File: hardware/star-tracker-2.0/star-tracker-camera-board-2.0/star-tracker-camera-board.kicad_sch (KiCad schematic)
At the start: 41 parts, among them J1 3-1734742-6, U1 AR0134CSSM00SPCA0, U2 TPS70618DRVR, U3 TPS71928-28DRVT, U4 TPS71928-28DRVT, X1 MC2520Z27.0000C19XSH

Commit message: Update to Camera Board
Update BOM for camera board, replaced lower tier dielectric caps to X7R
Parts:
- C1: DIS Digikey -> Mouser; DPN 399-19365-1-ND -> 81-GXT155R71E103KE1D; MFR KEMET -> Murata; MPN C0402C103J5RACAUTO -> GXT155R71E103KE01D
- C11, C13, C7, C8, C9: DIS Digikey -> Mouser; DPN 399-17548-1-ND -> 80-C0402C104J4RAUTO
- C2, C3, C4, C5, C6: DIS Digikey -> Mouser; DPN 490-12286-1-ND -> 80-C0603C106J3RACTU; MFR Murata Electronics -> KEMET; MPN GRT188C81C106ME13D -> C0603C106J3RACTU
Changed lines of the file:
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@@
 			)
 		)
-		(property "Description" "10000 pF ±5% 50V Ceramic Capacitor X7R 0402 (1005 Metric)"
+		(property "Description" "0.01uF 10% 25VDC Ceramic Capacitor X7R 0402 (1005 Metric)"
 			(at 58.42 68.58 0)
 			(hide yes)
@@
 			)
 		)
-		(property "DIS" "Digikey"
+		(property "DIS" "Mouser"
 			(at 58.42 68.58 0)
 			(hide yes)
@@
 			)
 		)
-		(property "DPN" "399-19365-1-ND"
+		(property "DPN" "81-GXT155R71E103KE1D "
 			(at 58.42 68.58 0)
 			(hide yes)
@@
 			)
 		)
-		(property "MFR" "KEMET"
+		(property "MFR" "Murata"
 			(at 58.42 68.58 0)
 			(hide yes)
@@
 			)
 		)
-		(property "MPN" "C0402C103J5RACAUTO"
+		(property "MPN" "GXT155R71E103KE01D"
 			(at 58.42 68.58 0)
 			(hide yes)
@@
 			)
 		)
-		(property "Description" "10 µF ±20% 16V Ceramic Capacitor X6S 0603 (1608 Metric)"
+		(property "Description" "10 µF ±5% 23V Ceramic Capacitor X7R 0603 (1608 Metric)"
 			(at 314.96 50.8 0)
 			(hide yes)
@@
 			)
 		)
-		(property "DIS" "Digikey"
+		(property "DIS" "Mouser"
 			(at 314.96 50.8 0)
 			(hide yes)
@@
 			)
 		)
-		(property "DPN" "490-12286-1-ND"
+		(property "DPN" "80-C0603C106J3RACTU"
 			(at 314.96 50.8 0)
 			(hide yes)
@@
 			)
 		)
-		(property "MFR" "Murata Electronics"
+		(property "MFR" "KEMET"
 			(at 314.96 50.8 0)
 			(hide yes)
@@
 			)
 		)
-		(property "MPN" "GRT188C81C106ME13D"
+		(property "MPN" "C0603C106J3RACTU "
 			(at 314.96 50.8 0)
 			(hide yes)
@@
 			)
 		)
-		(property "DIS" "Digikey"
+		(property "DIS" "Mouser"
 			(at 368.3 50.8 0)
 			(hide yes)
@@
 			)
 		)
-		(property "DPN" "399-17548-1-ND"
+		(property "DPN" "80-C0402C104J4RAUTO "
 			(at 368.3 50.8 0)
 			(hide yes)
@@
 			)
 		)
-		(property "Description" "10 µF ±20% 16V Ceramic Capacitor X6S 0603 (1608 Metric)"
+		(property "Description" "10 µF ±5% 23V Ceramic Capacitor X7R 0603 (1608 Metric)"
 			(at 304.8 50.8 0)
 			(hide yes)
@@
 			)
 		)
-		(property "DIS" "Digikey"
+		(property "DIS" "Mouser"
 			(at 304.8 50.8 0)
 			(hide yes)
@@
 			)
 		)
-		(property "DPN" "490-12286-1-ND"
+		(property "DPN" "80-C0603C106J3RACTU"
 			(at 304.8 50.8 0)
 			(hide yes)
@@
 			)
 		)
-		(property "MFR" "Murata Electronics"
+		(property "MFR" "KEMET"
 			(at 304.8 50.8 0)
 			(hide yes)
@@
 			)
 		)
-		(property "MPN" "GRT188C81C106ME13D"
+		(property "MPN" "C0603C106J3RACTU "
 			(at 304.8 50.8 0)
 			(hide yes)
@@
 			)
 		)
-		(property "Description" "10 µF ±20% 16V Ceramic Capacitor X6S 0603 (1608 Metric)"
+		(property "Description" "10 µF ±5% 23V Ceramic Capacitor X7R 0603 (1608 Metric)"
 			(at 284.48 50.8 0)
 			(hide yes)
@@
 			)
 		)
-		(property "DIS" "Digikey"
+		(property "DIS" "Mouser"
 			(at 284.48 50.8 0)
 			(hide yes)
@@
 			)
 		)
-		(property "DPN" "490-12286-1-ND"
+		(property "DPN" "80-C0603C106J3RACTU"
 			(at 284.48 50.8 0)
 			(hide yes)
@@
 			)
 		)
-		(property "MFR" "Murata Electronics"
+		(property "MFR" "KEMET"
 			(at 284.48 50.8 0)
 			(hide yes)
@@
 			)
 		)
-		(property "MPN" "GRT188C81C106ME13D"
+		(property "MPN" "C0603C106J3RACTU "
 			(at 284.48 50.8 0)
 			(hide yes)
@@
 			)
 		)
-		(property "DIS" "Digikey"
+		(property "DIS" "Mouser"
 			(at 327.66 50.8 0)
 			(hide yes)
@@
 			)
 		)
-		(property "DPN" "399-17548-1-ND"
+		(property "DPN" "80-C0402C104J4RAUTO "
 			(at 327.66 50.8 0)
 			(hide yes)
@@
 			)
 		)
-		(property "Description" "10 µF ±20% 16V Ceramic Capacitor X6S 0603 (1608 Metric)"
+		(property "Description" "10 µF ±5% 23V Ceramic Capacitor X7R 0603 (1608 Metric)"
 			(at 274.32 50.8 0)
 			(hide yes)
@@
 			)
 		)
-		(property "DIS" "Digikey"
+		(property "DIS" "Mouser"
 			(at 274.32 50.8 0)
 			(hide yes)
@@
 			)
 		)
-		(property "DPN" "490-12286-1-ND"
+		(property "DPN" "80-C0603C106J3RACTU"
 			(at 274.32 50.8 0)
 			(hide yes)
@@
 			)
 		)
-		(property "MFR" "Murata Electronics"
+		(property "MFR" "KEMET"
 			(at 274.32 50.8 0)
 			(hide yes)
@@
 			)
 		)
-		(property "MPN" "GRT188C81C106ME13D"
+		(property "MPN" "C0603C106J3RACTU "
 			(at 274.32 50.8 0)
 			(hide yes)
@@
 			)
 		)
-		(property "Description" "10 µF ±20% 16V Ceramic Capacitor X6S 0603 (1608 Metric)"
+		(property "Description" "10 µF ±5% 23V Ceramic Capacitor X7R 0603 (1608 Metric)"
 			(at 294.64 50.8 0)
 			(hide yes)
@@
 			)
 		)
-		(property "DIS" "Digikey"
+		(property "DIS" "Mouser"
 			(at 294.64 50.8 0)
 			(hide yes)
@@
 			)
 		)
-		(property "DPN" "490-12286-1-ND"
+		(property "DPN" "80-C0603C106J3RACTU"
 			(at 294.64 50.8 0)
 			(hide yes)
@@
 			)
 		)
-		(property "MFR" "Murata Electronics"
+		(property "MFR" "KEMET"
 			(at 294.64 50.8 0)
 			(hide yes)
@@
 			)
 		)
-		(property "MPN" "GRT188C81C106ME13D"
+		(property "MPN" "C0603C106J3RACTU "
 			(at 294.64 50.8 0)
 			(hide yes)
@@
 			)
 		)
-		(property "DIS" "Digikey"
+		(property "DIS" "Mouser"
 			(at 358.14 50.8 0)
 			(hide yes)
@@
 			)
 		)
-		(property "DPN" "399-17548-1-ND"
+		(property "DPN" "80-C0402C104J4RAUTO "
 			(at 358.14 50.8 0)
 			(hide yes)
@@
 			)
 		)
-		(property "DIS" "Digikey"
+		(property "DIS" "Mouser"
 			(at 337.82 50.8 0)
 			(hide yes)
@@
 			)
 		)
-		(property "DPN" "399-17548-1-ND"
+		(property "DPN" "80-C0402C104J4RAUTO "
 			(at 337.82 50.8 0)
 			(hide yes)
@@
 			)
 		)
-		(property "DIS" "Digikey"
+		(property "DIS" "Mouser"
 			(at 347.98 50.8 0)
 			(hide yes)
@@
 			)
 		)
-		(property "DPN" "399-17548-1-ND"
+		(property "DPN" "80-C0402C104J4RAUTO "
 			(at 347.98 50.8 0)
 			(hide yes)

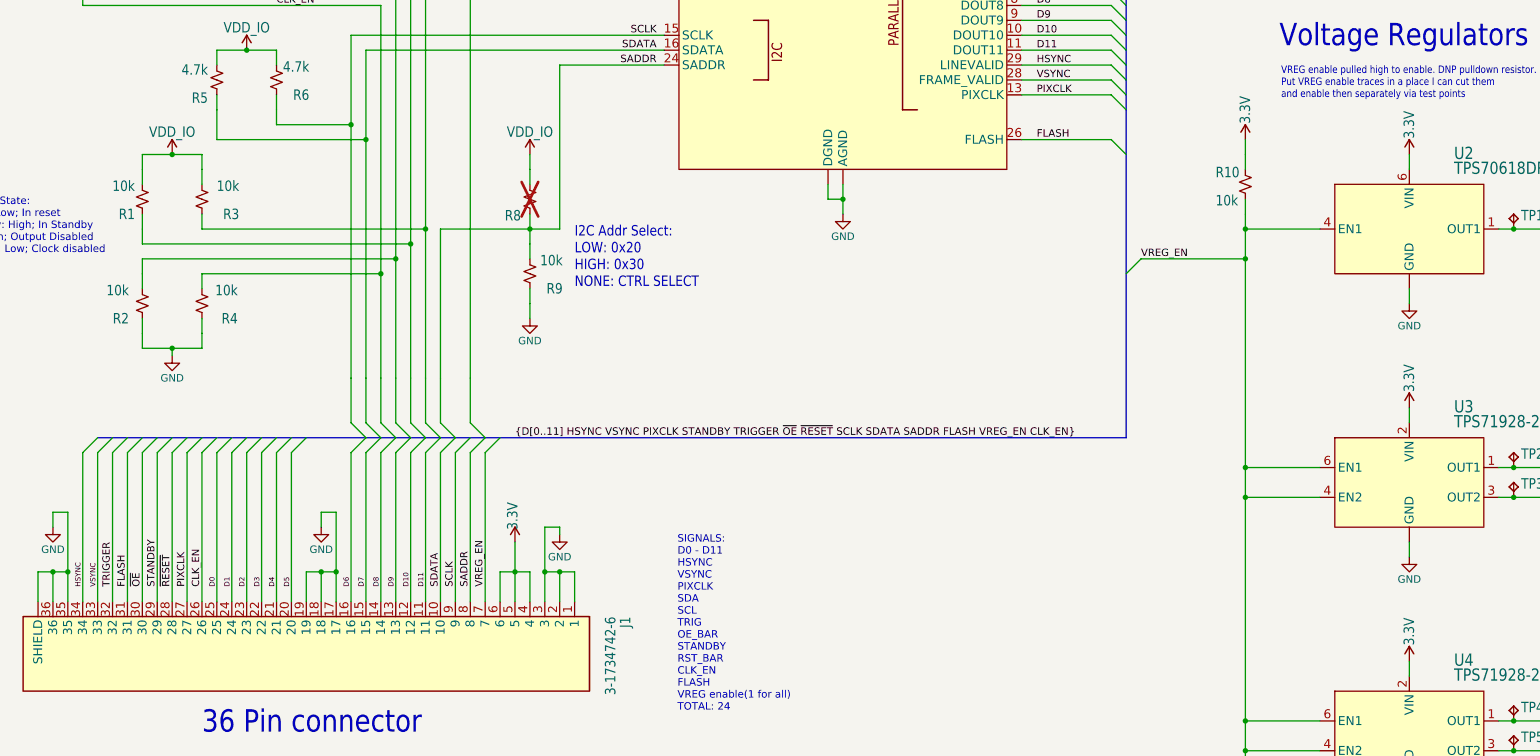
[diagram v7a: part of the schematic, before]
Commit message: Finishing touches
added gitignore for .ds_store (mac file for kicad) changed bom details for components. added 3d models to footprints. Went over schematic checklist. Camera and star tracker ready for final DR for send off.
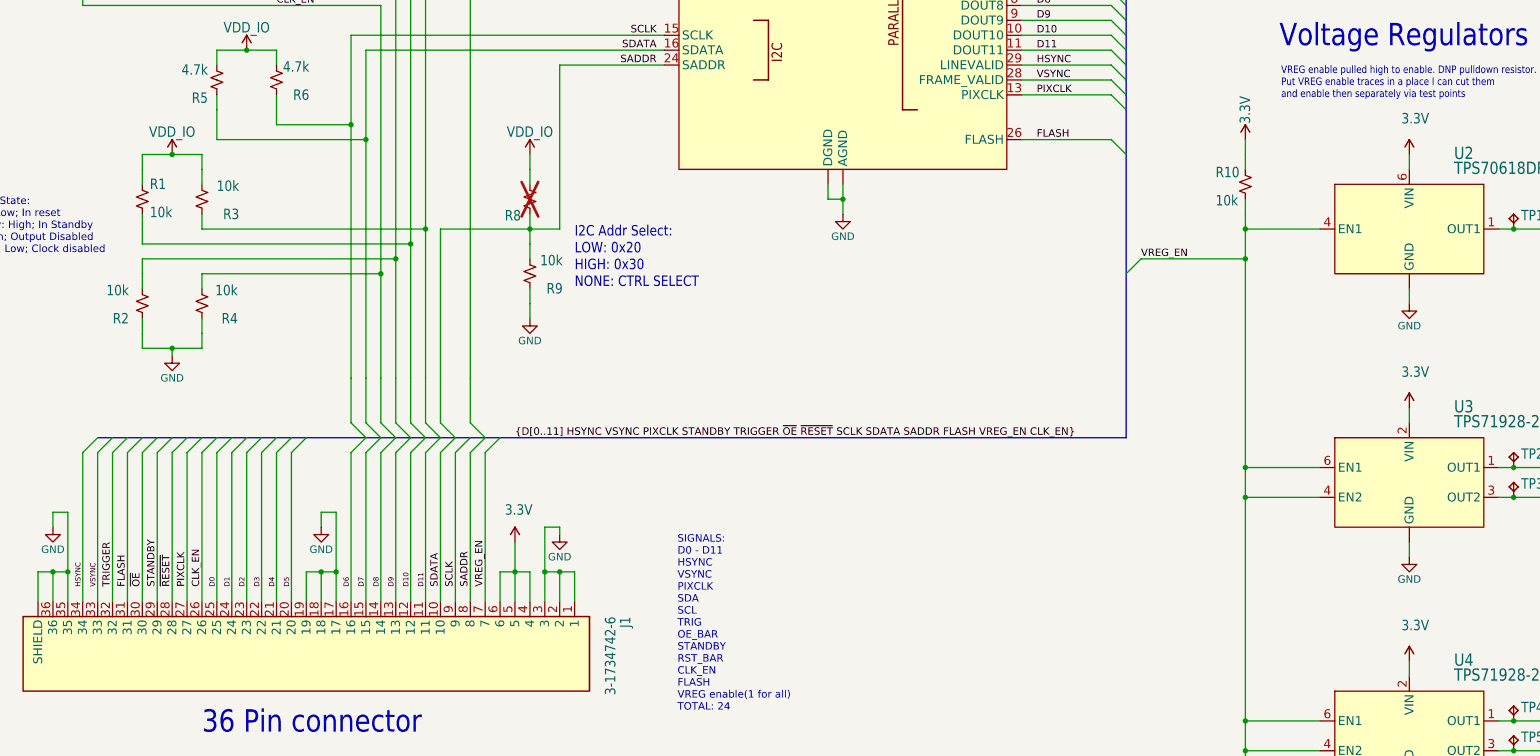
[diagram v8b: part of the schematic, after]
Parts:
- C10, C12, C15, C17, C19: DIS DigiKey -> Mouser; DPN 490-GRT188C71E225KE13DCT-ND -> 81-GRT188C71E225KE3D
- C14, C16, C18: DIS DigiKey -> Mouser; DPN 490-18215-1-ND -> 81-GRT155C81E105KE3D
- J1: DPN A100241CT-ND -> 17-3-2492144-6TR-ND; MPN 3-1734742-6 -> 3-2492144-6
- R1, R10, R2, R3, R4, R9: DIS Digikey -> Mouser; DPN RMCF0402FT10K0CT-ND -> 708-RMCF0402FT10K0; MPN RMCF0402FT10K0 -> RMCF0402FT10K0
- R5, R6: DIS Digikey -> Mouser; DPN RMCF0402FT4K70CT-ND -> 708-RMCF0402FT4K70
- R7: DIS Digikey -> Mouser; DPN RMCF0402FT100RCT-ND -> 708-RMCF0402FT100R
- U1: DIS DigiKey -> Mouser
- U2: DIS DigiKey -> Mouser; DPN 296-48768-1-ND -> 595-TPS70618DRVR; MPN TPS70618DRVR -> TPS70618DRVR
- U3, U4: DIS DigiKey -> Mouser; DPN 296-TPS71928-28DRVTCT-ND -> 595-TPS71928-28DRVT
- X1: DIS DigiKey -> Mouser; DPN 478-MC2520Z27.0000C19XSHCT-ND -> 346-MC2520Z27.0000C1; MPN MC2520Z27.0000C19XSH -> MC2520Z27.0000C19XSH
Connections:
- net STANDBY: now also R1.2; no longer R1.1
- net VDD_IO: now also R1.1; no longer R1.2
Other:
- moved on the sheet: R1
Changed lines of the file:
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@@
 	(title_block
 		(title "Oresat Star Tracker Camera Board")
-		(date "2026-04-22")
-		(rev "4.1")
+		(date "2026-06-19")
+		(rev "4.2")
 		(company "Portland State Aerospace Society")
 	)
@@
 			)
 		)
-		(property "DIS" "DigiKey"
+		(property "DIS" "Mouser"
 			(at 358.14 193.04 0)
 			(hide yes)
@@
 			)
 		)
-		(property "DPN" "490-GRT188C71E225KE13DCT-ND"
+		(property "DPN" "81-GRT188C71E225KE3D "
 			(at 358.14 193.04 0)
 			(hide yes)
@@
 			)
 		)
-		(property "DIS" "Digikey"
+		(property "DIS" "Mouser"
 			(at 78.74 144.78 0)
 			(hide yes)
@@
 			)
 		)
-		(property "DPN" "RMCF0402FT10K0CT-ND"
+		(property "DPN" "708-RMCF0402FT10K0 "
 			(at 78.74 144.78 0)
 			(hide yes)
@@
 			)
 		)
-		(property "MPN" "RMCF0402FT10K0"
+		(property "MPN" "RMCF0402FT10K0 "
 			(at 78.74 144.78 0)
 			(hide yes)
@@
 			)
 		)
-		(property "Description" "36 Position FFC, FPC Connector Contacts, Vertical, 1 Sided 0.020\" (0.50mm) Surface Mount"
+		(property "Description" "36 Position FPC Connector Contacts, Vertical - 2 Sided 0.020\" (0.50mm) Surface Mount"
 			(at 101.6 205.74 0)
 			(hide yes)
@@
 			)
 		)
-		(property "DPN" "A100241CT-ND"
+		(property "DPN" "17-3-2492144-6TR-ND"
 			(at 101.6 205.74 0)
 			(hide yes)
@@
 			)
 		)
-		(property "MPN" "3-1734742-6"
+		(property "MPN" "3-2492144-6"
 			(at 101.6 205.74 0)
 			(hide yes)
@@
 			)
 		)
-		(property "DIS" "Digikey"
+		(property "DIS" "Mouser"
 			(at 88.9 144.78 0)
 			(hide yes)
@@
 			)
 		)
-		(property "DPN" "RMCF0402FT10K0CT-ND"
+		(property "DPN" "708-RMCF0402FT10K0 "
 			(at 88.9 144.78 0)
 			(hide yes)
@@
 			)
 		)
-		(property "MPN" "RMCF0402FT10K0"
+		(property "MPN" "RMCF0402FT10K0 "
 			(at 88.9 144.78 0)
 			(hide yes)
@@
 			)
 		)
-		(property "DIS" "Digikey"
+		(property "DIS" "Mouser"
 			(at 110.49 66.04 0)
 			(hide yes)
@@
 			)
 		)
-		(property "DPN" "RMCF0402FT100RCT-ND"
+		(property "DPN" "708-RMCF0402FT100R "
 			(at 110.49 66.04 0)
 			(hide yes)
@@
 			)
 		)
-		(property "DIS" "DigiKey"
+		(property "DIS" "Mouser"
 			(at 347.98 193.04 0)
 			(hide yes)
@@
 			)
 		)
-		(property "DPN" "490-GRT188C71E225KE13DCT-ND"
+		(property "DPN" "81-GRT188C71E225KE3D "
 			(at 347.98 193.04 0)
 			(hide yes)
@@
 			)
 		)
-		(property "DIS" "Digikey"
+		(property "DIS" "Mouser"
 			(at 91.44 106.68 0)
 			(hide yes)
@@
 			)
 		)
-		(property "DPN" "RMCF0402FT4K70CT-ND"
+		(property "DPN" "708-RMCF0402FT4K70 "
 			(at 91.44 106.68 0)
 			(hide yes)
@@
 			)
 		)
-		(property "DIS" "DigiKey"
+		(property "DIS" "Mouser"
 			(at 378.46 137.16 0)
 			(hide yes)
@@
 			)
 		)
-		(property "DPN" "490-18215-1-ND"
+		(property "DPN" "81-GRT155C81E105KE3D"
 			(at 378.46 137.16 0)
 			(hide yes)
@@
 			)
 		)
-		(property "DIS" "DigiKey"
+		(property "DIS" "Mouser"
 			(at 294.64 218.44 0)
 			(hide yes)
@@
 			)
 		)
-		(property "DPN" "296-TPS71928-28DRVTCT-ND"
+		(property "DPN" "595-TPS71928-28DRVT "
 			(at 294.64 218.44 0)
 			(hide yes)
@@
 			)
 		)
-		(property "DIS" "DigiKey"
+		(property "DIS" "Mouser"
 			(at 294.64 132.08 0)
 			(hide yes)
@@
 			)
 		)
-		(property "DPN" "296-48768-1-ND"
+		(property "DPN" "595-TPS70618DRVR "
 			(at 294.64 132.08 0)
 			(hide yes)
@@
 			)
 		)
-		(property "MPN" "TPS70618DRVR"
+		(property "MPN" "TPS70618DRVR "
 			(at 294.64 132.08 0)
 			(hide yes)
@@
 			)
 		)
-		(property "DIS" "Digikey"
+		(property "DIS" "Mouser"
 			(at 144.78 139.7 0)
 			(hide yes)
@@
 			)
 		)
-		(property "DPN" "RMCF0402FT10K0CT-ND"
+		(property "DPN" "708-RMCF0402FT10K0 "
 			(at 144.78 139.7 0)
 			(hide yes)
@@
 			)
 		)
-		(property "MPN" "RMCF0402FT10K0"
+		(property "MPN" "RMCF0402FT10K0 "
 			(at 144.78 139.7 0)
 			(hide yes)
@@
 			)
 		)
-		(property "DIS" "Digikey"
+		(property "DIS" "Mouser"
 			(at 101.6 106.68 0)
 			(hide yes)
@@
 			)
 		)
-		(property "DPN" "RMCF0402FT4K70CT-ND"
+		(property "DPN" "708-RMCF0402FT4K70 "
 			(at 101.6 106.68 0)
 			(hide yes)
@@
 		)
 		(property "Value" "3.3V"
-			(at 295.656 157.48 90)
+			(at 295.656 157.48 0)
 			(show_name no)
 			(do_not_autoplace no)
@@
 			)
 		)
-		(property "DIS" "DigiKey"
+		(property "DIS" "Mouser"
 			(at 378.46 193.04 0)
 			(hide yes)
@@
 			)
 		)
-		(property "DPN" "490-GRT188C71E225KE13DCT-ND"
+		(property "DPN" "81-GRT188C71E225KE3D "
 			(at 378.46 193.04 0)
 			(hide yes)
@@
 			)
 		)
-		(property "DIS" "DigiKey"
+		(property "DIS" "Mouser"
 			(at 198.12 91.44 0)
 			(hide yes)
@@
 			)
 		)
-		(property "DIS" "DigiKey"
+		(property "DIS" "Mouser"
 			(at 388.62 193.04 0)
 			(hide yes)
@@
 			)
 		)
-		(property "DPN" "490-GRT188C71E225KE13DCT-ND"
+		(property "DPN" "81-GRT188C71E225KE3D "
 			(at 388.62 193.04 0)
 			(hide yes)
@@
 			)
 		)
-		(property "DIS" "DigiKey"
+		(property "DIS" "Mouser"
 			(at 368.3 193.04 0)
 			(hide yes)
@@
 			)
 		)
-		(property "DPN" "490-GRT188C71E225KE13DCT-ND"
+		(property "DPN" "81-GRT188C71E225KE3D "
 			(at 368.3 193.04 0)
 			(hide yes)
@@
 			)
 		)
-		(property "DIS" "DigiKey"
+		(property "DIS" "Mouser"
 			(at 368.3 137.16 0)
 			(hide yes)
@@
 			)
 		)
-		(property "DPN" "490-18215-1-ND"
+		(property "DPN" "81-GRT155C81E105KE3D"
 			(at 368.3 137.16 0)
 			(hide yes)
@@
 		)
 		(property "Value" "3.3V"
-			(at 295.656 114.3 90)
+			(at 295.656 114.3 0)
 			(show_name no)
 			(do_not_autoplace no)
@@
 			)
 		)
-		(property "DIS" "DigiKey"
+		(property "DIS" "Mouser"
 			(at 294.64 175.26 0)
 			(hide yes)
@@
 			)
 		)
-		(property "DPN" "296-TPS71928-28DRVTCT-ND"
+		(property "DPN" "595-TPS71928-28DRVT "
 			(at 294.64 175.26 0)
 			(hide yes)
@@
 			)
 		)
-		(property "DIS" "DigiKey"
+		(property "DIS" "Mouser"
 			(at 88.9 66.04 0)
 			(hide yes)
@@
 			)
 		)
-		(property "DPN" "478-MC2520Z27.0000C19XSHCT-ND"
+		(property "DPN" "346-MC2520Z27.0000C1"
 			(at 88.9 66.04 0)
 			(hide yes)
@@
 			)
 		)
-		(property "MPN" "MC2520Z27.0000C19XSH"
+		(property "MPN" "MC2520Z27.0000C19XSH "
 			(at 88.9 66.04 0)
 			(hide yes)
@@
 			)
 		)
-		(property "DIS" "DigiKey"
+		(property "DIS" "Mouser"
 			(at 388.62 137.16 0)
 			(hide yes)
@@
 			)
 		)
-		(property "DPN" "490-18215-1-ND"
+		(property "DPN" "81-GRT155C81E105KE3D"
 			(at 388.62 137.16 0)
 			(hide yes)
@@
 	(symbol
 		(lib_id "Device:R_Small_US")
-		(at 78.74 127 180)
+		(at 78.74 127 0)
 		(unit 1)
 		(body_style 1)
@@
 		(dnp no)
 		(property "Reference" "R1"
-			(at 77.47 128.524 0)
+			(at 80.01 125.476 0)
 			(show_name no)
 			(do_not_autoplace no)
@@
 		)
 		(property "Value" "10k"
-			(at 77.47 123.7234 0)
+			(at 80.01 130.2766 0)
 			(show_name no)
 			(do_not_autoplace no)
@@
 			)
 		)
-		(property "DIS" "Digikey"
+		(property "DIS" "Mouser"
 			(at 78.74 127 0)
 			(hide yes)
@@
 			)
 		)
-		(property "DPN" "RMCF0402FT10K0CT-ND"
+		(property "DPN" "708-RMCF0402FT10K0 "
 			(at 78.74 127 0)
 			(hide yes)
@@
 			)
 		)
-		(property "MPN" "RMCF0402FT10K0"
+		(property "MPN" "RMCF0402FT10K0 "
 			(at 78.74 127 0)
 			(hide yes)
@@
 		)
 		(property "Value" "3.3V"
-			(at 295.656 200.66 90)
+			(at 295.656 200.66 0)
 			(show_name no)
 			(do_not_autoplace no)
@@
 			)
 		)
-		(property "DIS" "Digikey"
+		(property "DIS" "Mouser"
 			(at 88.9 127 0)
 			(hide yes)
@@
 			)
 		)
-		(property "DPN" "RMCF0402FT10K0CT-ND"
+		(property "DPN" "708-RMCF0402FT10K0 "
 			(at 88.9 127 0)
 			(hide yes)
@@
 			)
 		)
-		(property "MPN" "RMCF0402FT10K0"
+		(property "MPN" "RMCF0402FT10K0 "
 			(at 88.9 127 0)
 			(hide yes)
@@
 			)
 		)
-		(property "DIS" "Digikey"
+		(property "DIS" "Mouser"
 			(at 266.7 124.46 0)
 			(hide yes)
@@
 			)
 		)
-		(property "DPN" "RMCF0402FT10K0CT-ND"
+		(property "DPN" "708-RMCF0402FT10K0 "
 			(at 266.7 124.46 0)
 			(hide yes)
@@
 			)
 		)
-		(property "MPN" "RMCF0402FT10K0"
+		(property "MPN" "RMCF0402FT10K0 "
 			(at 266.7 124.46 0)
 			(hide yes)
@@
 		)
 		(property "Value" "3.3V"
-			(at 142.875 180.975 90)
+			(at 142.875 180.975 0)
 			(show_name no)
 			(do_not_autoplace no)
